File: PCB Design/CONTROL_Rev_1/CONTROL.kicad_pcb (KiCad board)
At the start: 2 copper layers, 40 x 80 mm, 50 parts, among them J1 Conn_01x24_Pin, J2 Conn_01x24_Pin, J3 Micro_SD_Card, J4 USB_C_Receptacle_USB2.0_16P, SW1 SW_SPDT, U1 STM32F446RET6, U2 USBLC6-2SC6, Y1 16MHz, Y2 32.768KHz

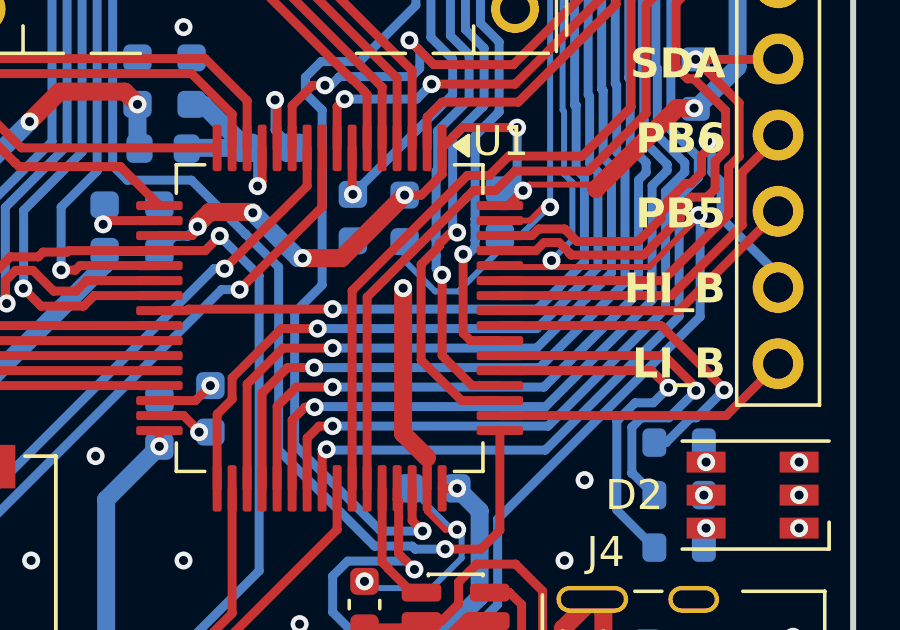
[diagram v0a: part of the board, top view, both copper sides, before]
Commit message: fix(uart): correct inter-MCU UART cross-connection
- Swap UART net labels on Pico side to correctly cross TX/RX
- Pico GPIO4 (pin 6): UART_TX -> UART_RX (connects to STM32 PA9/USART1_TX)
- Pico GPIO5 (pin 7): UART_RX -> UART_TX (connects to STM32 PA10/USART1_RX)
- Both MCUs confirmed on 3.3V — no level shifting required
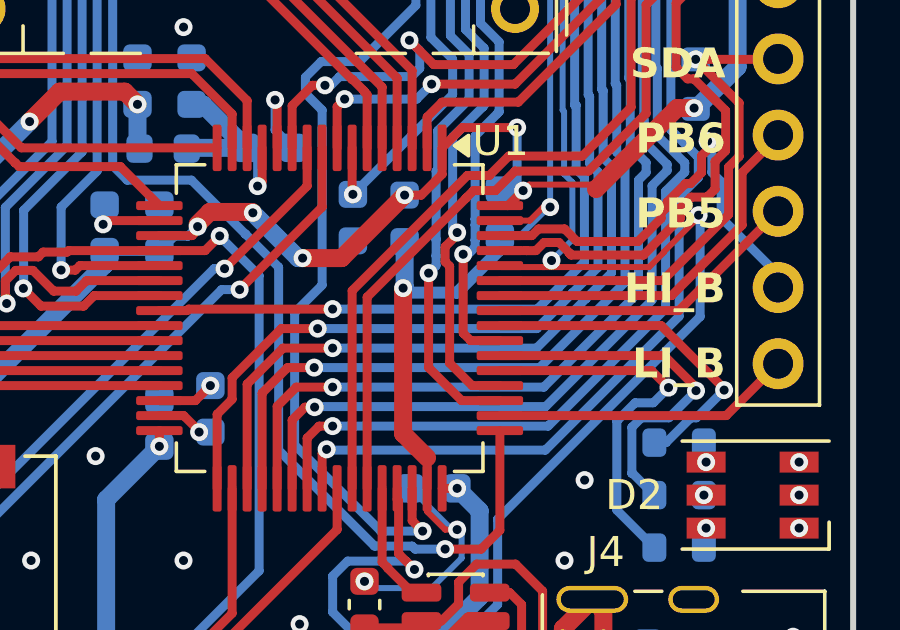
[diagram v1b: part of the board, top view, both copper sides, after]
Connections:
- A1 pad 1: /UART_TX -> /STM_UART_RX
- A1 pad 2: /UART_RX -> /STM_UART_TX
- U1 pad 51: /UART_TX -> /STM_UART_TX
- U1 pad 52: /UART_RX -> /STM_UART_RX
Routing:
- net /UART_TX: track 71.3 -> 0.00 mm, vias 1 -> 0
- net /STM_UART_RX: track 0.00 -> 69.8 mm, vias 0 -> 1
- net /STM_UART_TX: track 0.00 -> 67.8 mm, vias 0 -> 1
- net /UART_RX: track 66.9 -> 0.00 mm, vias 1 -> 0
- net GND: track 90.0 -> 90.8 mm

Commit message: fix(layout): move HSE and LSE crystals closer to STM32 OSC pins
- Relocate Y1 (16MHz HSE) directly above STM32 to reduce trace length
- Relocate Y2 (32.768kHz LSE) alongside Y1 above STM32
- C11/C12 load caps repositioned to follow crystals
- Shorter direct traces to PH0/PH1 and PC14/PC15 OSC pins
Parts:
- moved Y1 10.5 mm to (63.5, 147.9), turned to -90 degrees
- moved C12 8.52 mm to (66.3, 148.7), turned to 90 degrees
- moved Y2 6.08 mm to (68.6, 148.9), turned to -90 degrees
- moved C11 5.35 mm to (66.3, 145.4), turned to 90 degrees
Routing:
- net /HSE_OUT: track 19.3 -> 8.57 mm
- net /HSE_IN: track 23.6 -> 14.2 mm
- net /LSE_OUT: track 13.3 -> 5.88 mm
- net /LSE_IN: track 13.0 -> 7.33 mm
- net /PC3: track 63.2 -> 61.2 mm
- net GND: track 90.8 -> 89.5 mm, vias 131 -> 139
- net /SWDIO: track 47.5 -> 48.6 mm

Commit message: Added Control Board Outputs
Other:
- board text added: "CONTROL BOARD REV1.1 03/2026 By Samantha Chong"
- board text removed: "CONTROL BOARD REV1 03/2026 By Samantha Chong"
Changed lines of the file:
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@@
 			(drillshape 0)
 			(scaleselection 1)
-			(outputdirectory "CONTROL_BOARD_OUTPUT_08_018_2026/")
+			(outputdirectory "CONTROL_BOARD_OUTPUT_08_022_2026/")
 		)
 	)
@@
 		)
 	)
-	(gr_text "CONTROL BOARD \nREV1 03/2026\nBy Samantha Chong"
+	(gr_text "CONTROL BOARD \nREV1.1 03/2026\nBy Samantha Chong"
 		(at 67 176.9 0)
 		(layer "B.SilkS")

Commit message: CONTROL - Added 3D Models for Export
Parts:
- D2: footprint LED_SMD:LED_RGB_PLCC-6 -> CONTROL:LED_RGB_PLCC-6
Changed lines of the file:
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@@
 		)
 		(embedded_fonts no)
+		(model "${KIPRJMOD}/Library/LED_JE2835_CRW.step"
+			(offset
+				(xyz 0 0 0)
+			)
+			(scale
+				(xyz 1 1 1)
+			)
+			(rotate
+				(xyz -180 -180 -0)
+			)
+		)
 	)
 	(footprint "Capacitor_SMD:C_0603_1608Metric"
@@
 		)
 	)
-	(footprint "LED_SMD:LED_RGB_PLCC-6"
+	(footprint "CONTROL:LED_RGB_PLCC-6"
 		(layer "F.Cu")
 		(at 81.9 166.3 180)
@@
 		(tags "RGB LED PLCC-6")
 		(property "Reference" "D2"
-			(at 3.95 0 0)
+			(at 0 -2.55 0)
 			(layer "F.SilkS")
 			(effects
@@
 		)
 		(property "Value" "LED_RGB"
-			(at 0 2.8 0)
+			(at 0 2.8 180)
 			(layer "F.Fab")
 			(effects
@@
 		)
 		(embedded_fonts no)
-		(model "${KICAD9_3DMODEL_DIR}/LED_SMD.3dshapes/LED_RGB_PLCC-6.step"
+		(model "${KIPRJMOD}/Library/L1MC-RGB0028000MP0.stp"
 			(offset
-				(xyz 0 0 0)
+				(xyz 0 0 0.8)
 			)
 			(scale
@@
 			)
 			(rotate
-				(xyz 0 0 0)
+				(xyz -90 -0 -0)
 			)
 		)
@@
 		)
 		(embedded_fonts no)
+		(model "${KIPRJMOD}/Library/CJS-1200TB1.stp"
+			(offset
+				(xyz 0 0 2.5)
+			)
+			(scale
+				(xyz 1 1 1)
+			)
+			(rotate
+				(xyz -90 -0 -0)
+			)
+		)
 	)
 	(footprint "CONTROL:XTAL_ABS05W-32.768KHZ-D-2-T"
@@
 		)
 		(embedded_fonts no)
+		(model "${KIPRJMOD}/Library/LED_JE2835_CRW.step"
+			(offset
+				(xyz 0 0 0)
+			)
+			(scale
+				(xyz 1 1 1)
+			)
+			(rotate
+				(xyz -180 -180 -0)
+			)
+		)
 	)
 	(footprint "Resistor_SMD:R_0603_1608Metric"

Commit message: Updated
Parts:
- added J5: Micro_SD_Card, CONTROL:AMPHENOL_1140084168, F.Cu at (17.0, 30.4)
- added J6: USB_C_Receptacle_USB2.0_16P, Connector_USB:USB_C_Receptacle_GCT_USB4085, F.Cu at (15.8, -20.5)
- added REF**: MountingHole_2.2mm_M2, MountingHole:MountingHole_2.2mm_M2, F.Cu at (-17.0, 15.0)
- added REF**: MountingHole_2.2mm_M2, MountingHole:MountingHole_2.2mm_M2, F.Cu at (17.0, 15.0)
- added REF**: MountingHole_2.2mm_M2, MountingHole:MountingHole_2.2mm_M2, F.Cu at (-17.0, -15.0)
- added REF**: MountingHole_2.2mm_M2, MountingHole:MountingHole_2.2mm_M2, F.Cu at (17.0, -15.0)
- J1, J2: value Conn_01x24_Pin -> Conn_02x25_Odd_Even; footprint Connector_PinHeader_2.54mm:PinHeader_1x24_P2.54mm_Vertical -> CONTROL:HIROSE_DF40C-50DP-0.4V_51_
- J3: value Micro_SD_Card -> Conn_02x25_Odd_Even; footprint CONTROL:AMPHENOL_1140084168 -> CONTROL:HIROSE_DF40C-50DP-0.4V_51_; moved to B.Cu
- J4: value USB_C_Receptacle_USB2.0_16P -> Conn_02x25_Odd_Even; footprint Connector_USB:USB_C_Receptacle_GCT_USB4085 -> CONTROL:HIROSE_DF40C-50DP-0.4V_51_; moved to B.Cu
- R10, R8, R9: moved to F.Cu
- moved R12 206.7 mm to (10.8, -23.4), turned to 180 degrees
- moved R14 205.3 mm to (15.8, -18.6), turned to 0 degrees
- moved R11 203.8 mm to (14.9, -18.9), turned to 0 degrees
- moved U2 197.7 mm to (9.25, -16.9), turned to -90 degrees
- moved C21 195.0 mm to (11.9, -16.5)
- moved J4 186.5 mm to (17.0, 0.00), turned to -90 degrees
- moved J3 183.1 mm to (-17.0, 0.00)
- moved SW1 175.1 mm to (16.4, 9.25), turned to 180 degrees
- moved R1 172.0 mm to (14.0, 11.8), turned to 180 degrees
- moved D1 169.7 mm to (-15.8, 25.2), turned to 180 degrees
- moved D2 165.9 mm to (-16.6, 32.8), turned to 0 degrees
- moved R7 165.6 mm to (-12.8, 25.2), turned to 90 degrees
- moved R8 164.8 mm to (-12.1, 31.0), turned to 0 degrees
- moved R3 162.1 mm to (14.1, 4.50)
- moved R9 161.9 mm to (-12.1, 32.8), turned to 0 degrees
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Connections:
- J1 pad 1: 3.3V -> GND
- J1 pad 10: /GPIO_9 -> GND
- J1 pad 11: /GPIO_10 -> GND
- J1 pad 12: /GPIO_11 -> GND
- J1 pad 13: /GPIO_12 -> /GPIO_6
- J1 pad 14: /GPIO_13 -> /GPIO_6
- J1 pad 15: /GPIO_14 -> /GPIO_7
- J1 pad 16: /ADC1_IN0 -> /GPIO_7
- J1 pad 17: /ADC1_IN1 -> /GPIO_8
- J1 pad 18: /ADC1_IN2 -> /GPIO_8
- J1 pad 19: /ADC1_IN3 -> /GPIO_9
- J1 pad 20: /PC5 -> /GPIO_9
- J1 pad 21: /PB0 -> /GPIO_10
- J1 pad 22: /PB1 -> /GPIO_10
- J1 pad 23: /HI_A -> /GPIO_11
- J1 pad 24: /LI_A -> /GPIO_11
- J1 pad 3: 12V -> 3.3V
- J1 pad 4: GND -> 3.3V
- J1 pad 5: V_Piezo -> 3.3V
- J1 pad 6: GND -> 3.3V
- J1 pad 7: /GPIO_6 -> 3.3V
- J1 pad 8: /GPIO_7 -> 3.3V
- J1 pad 9: /GPIO_8 -> GND
- J2 pad 10: /PB12 -> /GPIO_27
- J2 pad 11: /PB14 -> /GPIO_26
- J2 pad 12: /PB15 -> /GPIO_26
- J2 pad 13: /PC6 -> /GPIO_17
- J2 pad 14: /PC7 -> /GPIO_17
- J2 pad 15: /PC8 -> /GPIO_16
- J2 pad 16: /PC9 -> /GPIO_16
- J2 pad 17: /PA9 -> /PC4
- J2 pad 18: /PA10 -> /PC4
- J2 pad 19: /SCL -> /PB12
- J2 pad 2: /PC0 -> /PC3
- J2 pad 20: /SDA -> /PB12
- J2 pad 21: /PB6 -> /PB14
- J2 pad 22: /PB5 -> /PB14
- J2 pad 23: /HI_B -> /PB15
- J2 pad 24: /LI_B -> /PB15
- J2 pad 3: /PC13 -> /PC0
- J2 pad 4: /GPIO_28 -> /PC0
- J2 pad 5: /GPIO_27 -> /PC13
- J2 pad 6: /GPIO_26 -> /PC13
- J2 pad 7: /GPIO_17 -> /GPIO_28
- J2 pad 8: /GPIO_16 -> /GPIO_28
- J2 pad 9: /PC4 -> /GPIO_27
- J3 pad 1: /DAT2 -> GND
- J3 pad 10: (no net) -> GND
- J3 pad 2: /CS -> GND
- J3 pad 3: /SPI2_MOSI -> 3.3V
- J3 pad 5: /SPI2_SCK -> 3.3V
- J3 pad 6: GND -> 3.3V
- J3 pad 7: /SPI2_MISO -> 3.3V
- J3 pad 8: /DAT1 -> 3.3V
- R11 pad 1: Net-(J4-CC1) -> Net-(J6-CC1)
- R12 pad 1: Net-(J4-CC2) -> Net-(J6-CC2)
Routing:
- net 3.3V: track 246.4 -> 6.47 mm, vias 17 -> 18
- net /HEARTBEAT: track 71.6 -> 0.00 mm, vias 3 -> 0
- net /STM_UART_RX: track 69.8 -> 0.00 mm, vias 1 -> 0
- net /STM_UART_TX: track 67.8 -> 0.00 mm, vias 1 -> 0
- net /SWCLK: track 59.1 -> 0.00 mm, vias 2 -> 0
- net GND: track 89.5 -> 33.1 mm, vias 139 -> 30
- net /SPI_SCK: track 54.8 -> 0.00 mm, vias 1 -> 0
- net /SPI_MOSI: track 54.5 -> 0.00 mm, vias 1 -> 0
- net /SPI_MISO: track 53.9 -> 0.00 mm, vias 1 -> 0
- net /SWDIO: track 48.6 -> 0.00 mm, vias 2 -> 0
- net /LI_A: track 14.7 -> 44.6 mm, vias 0 -> 5
- net /LI_B: track 9.99 -> 39.4 mm, vias 0 -> 3
- net /PB5: track 10.6 -> 39.0 mm, vias 0 -> 5
- net /SPI2_MOSI: track 28.7 -> 2.32 mm, vias 2 -> 1
- net /PB6: track 12.5 -> 38.9 mm, vias 0 -> 5
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- added copper zone on B.Cu, net 3.3V
- added copper zone on F.Cu, net 3.3V
- removed copper zone on B.Cu, net GND
- removed copper zone on F.Cu, net GND
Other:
- board size 40 x 80 mm -> 40 x 70 mm
- board text added: "BOARD TITLE REV2.0 05/2026 By S. Chong"
- board text added: "HEARTBEAT"
- board text added: "PICO"
- board text removed: "12V"
- board text removed: "3.3V"
- board text removed: "ADC1_IN0"
- board text removed: "ADC1_IN1"
- board text removed: "ADC1_IN2"
- board text removed: "ADC1_IN3"
- board text removed: "B0"
- board text removed: "B1"
- board text removed: "CONTROL BOARD REV1.1 03/2026 By Samantha Chong"
- board text removed: "GND"
- board text removed: "GPIO10"
- board text removed: "GPIO11"
- board text removed: "GPIO12"
- board text removed: "GPIO13"
- board text removed: "GPIO14"
- board text removed: "GPIO16"
- board text removed: "GPIO17"
- board text removed: "GPIO26"
- board text removed: "GPIO27"
- board text removed: "GPIO28"
- board text removed: "GPIO6"
- board text removed: "GPIO7"
- board text removed: "GPIO8"
- board text removed: "GPIO9"
- board text removed: "HI"
- board text removed: "HI_B"
- board text removed: "LI_A"
- board text removed: "LI_B"
- board text removed: "PA10"
- board text removed: "PA9"
- board text removed: "PB12"
- board text removed: "PB14"
- board text removed: "PB15"
- board text removed: "PB5"
- board text removed: "PB6"
- board text removed: "PC4"
- board text removed: "PC5"
- board text removed: "PC6"
- board text removed: "PC7"
- board text removed: "PC8"
- board text removed: "PC9"
- board text removed: "PG_12"
- board text removed: "PG_3.3"
- board text removed: "PG_VPi"
- board text removed: "SCL"
- board text removed: "SDA"
- board text removed: "V_Pi"

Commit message: Revert "Updated"
This reverts commit 89be44ed720659141c8ee702c54a520a60db740f.
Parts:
- removed J5: Micro_SD_Card, CONTROL:AMPHENOL_1140084168
- removed J6: USB_C_Receptacle_USB2.0_16P, Connector_USB:USB_C_Receptacle_GCT_USB4085
- removed REF** (x4): MountingHole_2.2mm_M2, MountingHole:MountingHole_2.2mm_M2
- J1, J2: value Conn_02x25_Odd_Even -> Conn_01x24_Pin; footprint CONTROL:HIROSE_DF40C-50DP-0.4V_51_ -> Connector_PinHeader_2.54mm:PinHeader_1x24_P2.54mm_Vertical
- J3: value Conn_02x25_Odd_Even -> Micro_SD_Card; footprint CONTROL:HIROSE_DF40C-50DP-0.4V_51_ -> CONTROL:AMPHENOL_1140084168; moved to F.Cu
- J4: value Conn_02x25_Odd_Even -> USB_C_Receptacle_USB2.0_16P; footprint CONTROL:HIROSE_DF40C-50DP-0.4V_51_ -> Connector_USB:USB_C_Receptacle_GCT_USB4085; moved to F.Cu
- R10, R8, R9: moved to B.Cu
- moved R12 206.7 mm to (78.4, 172.0), turned to 90 degrees
- moved R14 205.3 mm to (72.9, 178.5), turned to 180 degrees
- moved R11 203.8 mm to (73.9, 176.2), turned to -90 degrees
- moved U2 197.7 mm to (72.0, 170.5), turned to 180 degrees
- moved C21 195.0 mm to (69.0, 169.9)
- moved J4 186.5 mm to (75.6, 177.1), turned to 90 degrees
- moved J3 183.1 mm to (48.5, 171.0)
- moved SW1 175.1 mm to (67.5, 176.8), turned to 0 degrees
- moved R1 172.0 mm to (69.7, 174.5), turned to 0 degrees
- moved D1 169.7 mm to (62.1, 176.0), turned to -90 degrees
- moved D2 165.9 mm to (81.9, 166.3), turned to 180 degrees
- moved R7 165.6 mm to (62.1, 173.0), turned to 180 degrees
- moved R8 164.8 mm to (79.5, 168.1), turned to 180 degrees
- moved R3 162.1 mm to (80.0, 152.6)
- moved R9 161.9 mm to (79.5, 166.3), turned to 180 degrees
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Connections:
- J1 pad 1: GND -> 3.3V
- J1 pad 10: GND -> /GPIO_9
- J1 pad 11: GND -> /GPIO_10
- J1 pad 12: GND -> /GPIO_11
- J1 pad 13: /GPIO_6 -> /GPIO_12
- J1 pad 14: /GPIO_6 -> /GPIO_13
- J1 pad 15: /GPIO_7 -> /GPIO_14
- J1 pad 16: /GPIO_7 -> /ADC1_IN0
- J1 pad 17: /GPIO_8 -> /ADC1_IN1
- J1 pad 18: /GPIO_8 -> /ADC1_IN2
- J1 pad 19: /GPIO_9 -> /ADC1_IN3
- J1 pad 20: /GPIO_9 -> /PC5
- J1 pad 21: /GPIO_10 -> /PB0
- J1 pad 22: /GPIO_10 -> /PB1
- J1 pad 23: /GPIO_11 -> /HI_A
- J1 pad 24: /GPIO_11 -> /LI_A
- J1 pad 3: 3.3V -> 12V
- J1 pad 4: 3.3V -> GND
- J1 pad 5: 3.3V -> V_Piezo
- J1 pad 6: 3.3V -> GND
- J1 pad 7: 3.3V -> /GPIO_6
- J1 pad 8: 3.3V -> /GPIO_7
- J1 pad 9: GND -> /GPIO_8
- J2 pad 10: /GPIO_27 -> /PB12
- J2 pad 11: /GPIO_26 -> /PB14
- J2 pad 12: /GPIO_26 -> /PB15
- J2 pad 13: /GPIO_17 -> /PC6
- J2 pad 14: /GPIO_17 -> /PC7
- J2 pad 15: /GPIO_16 -> /PC8
- J2 pad 16: /GPIO_16 -> /PC9
- J2 pad 17: /PC4 -> /PA9
- J2 pad 18: /PC4 -> /PA10
- J2 pad 19: /PB12 -> /SCL
- J2 pad 2: /PC3 -> /PC0
- J2 pad 20: /PB12 -> /SDA
- J2 pad 21: /PB14 -> /PB6
- J2 pad 22: /PB14 -> /PB5
- J2 pad 23: /PB15 -> /HI_B
- J2 pad 24: /PB15 -> /LI_B
- J2 pad 3: /PC0 -> /PC13
- J2 pad 4: /PC0 -> /GPIO_28
- J2 pad 5: /PC13 -> /GPIO_27
- J2 pad 6: /PC13 -> /GPIO_26
- J2 pad 7: /GPIO_28 -> /GPIO_17
- J2 pad 8: /GPIO_28 -> /GPIO_16
- J2 pad 9: /GPIO_27 -> /PC4
- J3 pad 1: GND -> /DAT2
- J3 pad 10: GND -> (no net)
- J3 pad 2: GND -> /CS
- J3 pad 3: 3.3V -> /SPI2_MOSI
- J3 pad 5: 3.3V -> /SPI2_SCK
- J3 pad 6: 3.3V -> GND
- J3 pad 7: 3.3V -> /SPI2_MISO
- J3 pad 8: 3.3V -> /DAT1
- R11 pad 1: Net-(J6-CC1) -> Net-(J4-CC1)
- R12 pad 1: Net-(J6-CC2) -> Net-(J4-CC2)
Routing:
- net 3.3V: track 6.47 -> 246.4 mm, vias 18 -> 17
- net /HEARTBEAT: track 0.00 -> 71.6 mm, vias 0 -> 3
- net /STM_UART_RX: track 0.00 -> 69.8 mm, vias 0 -> 1
- net /STM_UART_TX: track 0.00 -> 67.8 mm, vias 0 -> 1
- net /SWCLK: track 0.00 -> 59.1 mm, vias 0 -> 2
- net GND: track 33.1 -> 89.5 mm, vias 30 -> 139
- net /SPI_SCK: track 0.00 -> 54.8 mm, vias 0 -> 1
- net /SPI_MOSI: track 0.00 -> 54.5 mm, vias 0 -> 1
- net /SPI_MISO: track 0.00 -> 53.9 mm, vias 0 -> 1
- net /SWDIO: track 0.00 -> 48.6 mm, vias 0 -> 2
- net /LI_A: track 44.6 -> 14.7 mm, vias 5 -> 0
- net /LI_B: track 39.4 -> 9.99 mm, vias 3 -> 0
- net /PB5: track 39.0 -> 10.6 mm, vias 5 -> 0
- net /SPI2_MOSI: track 2.32 -> 28.7 mm, vias 1 -> 2
- net /PB6: track 38.9 -> 12.5 mm, vias 5 -> 0
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- added copper zone on B.Cu, net GND
- added copper zone on F.Cu, net GND
- removed copper zone on B.Cu, net 3.3V
- removed copper zone on F.Cu, net 3.3V
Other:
- board size 40 x 70 mm -> 40 x 80 mm
- board text added: "12V"
- board text added: "3.3V"
- board text added: "ADC1_IN0"
- board text added: "ADC1_IN1"
- board text added: "ADC1_IN2"
- board text added: "ADC1_IN3"
- board text added: "B0"
- board text added: "B1"
- board text added: "CONTROL BOARD REV1.1 03/2026 By Samantha Chong"
- board text added: "GND"
- board text added: "GPIO10"
- board text added: "GPIO11"
- board text added: "GPIO12"
- board text added: "GPIO13"
- board text added: "GPIO14"
- board text added: "GPIO16"
- board text added: "GPIO17"
- board text added: "GPIO26"
- board text added: "GPIO27"
- board text added: "GPIO28"
- board text added: "GPIO6"
- board text added: "GPIO7"
- board text added: "GPIO8"
- board text added: "GPIO9"
- board text added: "HI"
- board text added: "HI_B"
- board text added: "LI_A"
- board text added: "LI_B"
- board text added: "PA10"
- board text added: "PA9"
- board text added: "PB12"
- board text added: "PB14"
- board text added: "PB15"
- board text added: "PB5"
- board text added: "PB6"
- board text added: "PC4"
- board text added: "PC5"
- board text added: "PC6"
- board text added: "PC7"
- board text added: "PC8"
- board text added: "PC9"
- board text added: "PG_12"
- board text added: "PG_3.3"
- board text added: "PG_VPi"
- board text added: "SCL"
- board text added: "SDA"
- board text added: "V_Pi"
- board text removed: "BOARD TITLE REV2.0 05/2026 By S. Chong"
- board text removed: "HEARTBEAT"
- board text removed: "PICO"
